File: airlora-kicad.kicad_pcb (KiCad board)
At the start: 4 copper layers, 77 x 77 mm, 168 parts, among them IC1 BALFHB-WL-02D3, J1 12V, J10 I2C, J11 UART2, J2 Conn_Coaxial, J3 Led, J4 SHT, J5 I2C, J6 A_NO2, J7 UART1, J8 A_CO, J9 I2C, Q10 S8050, Q2 S8050, Q3 S8050, Q4 S8050, Q5 S8050, Q6 S8050, Q7 S8050, Q8 S8050, Q9 S8050, SW1 SW_Push, SW2 SW_Slide_DPDT, SW3 SW_Push, U1 TPS7A2633DRVR, U2 TPS54202DDC, U3 TPS7A2633DRVR, U4 BGS12WN6E6327, U6 STM32F103C8Tx, U7 STM32WLE5CCUx, X1 32MHZ, Y1 32.768kHz, Y2 8Mhz

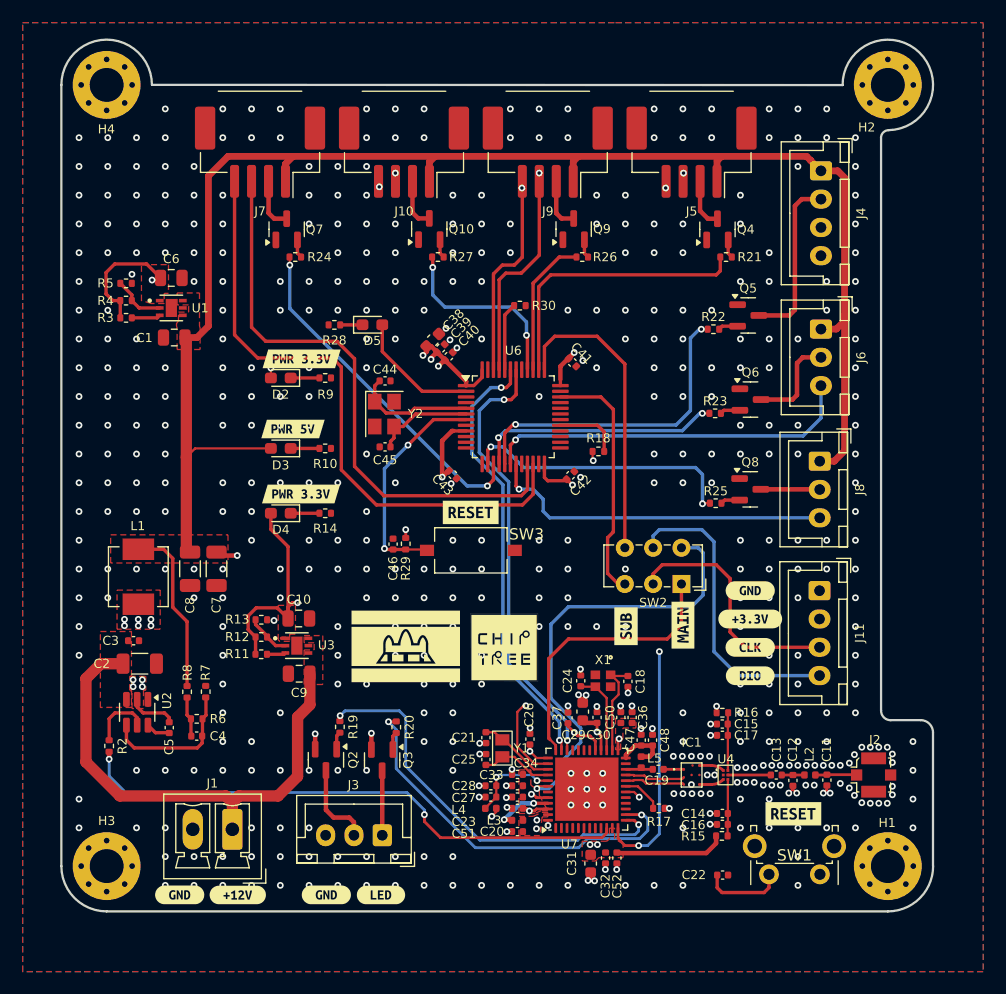
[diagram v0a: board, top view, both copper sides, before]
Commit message: Update trace and vias for power
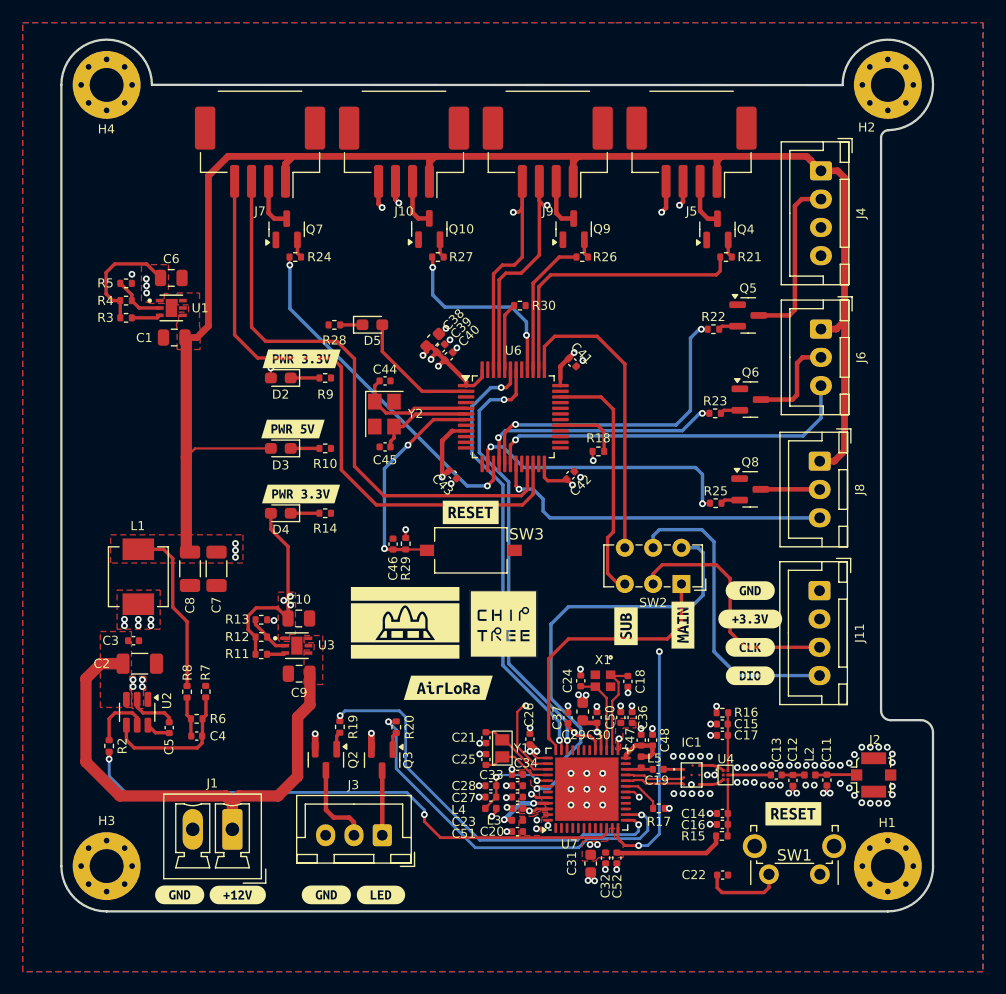
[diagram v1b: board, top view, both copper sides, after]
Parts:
- added kibuzzard-6679349C: G***, kibuzzard-6679349C, F.Cu at (94.7, 105.0)
- moved G*** 2.08 mm to (90.9, 99.3)
- moved G*** 2.08 mm to (99.6, 99.4)
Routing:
- net +3.3V_HP: track 74.7 -> 83.4 mm, vias 9 -> 11
- net /AirLora V3/MCU Sub/SDA1: track 61.7 -> 67.5 mm
- net +3.3V: track 106.0 -> 109.5 mm, vias 8 -> 11
- net /AirLora V3/MCU Sub/SCL1: track 60.7 -> 63.9 mm
- net +5V: track 186.8 -> 189.4 mm, vias 3 -> 5
- net GND: vias 484 -> 102

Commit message: Update power size track and add more vias
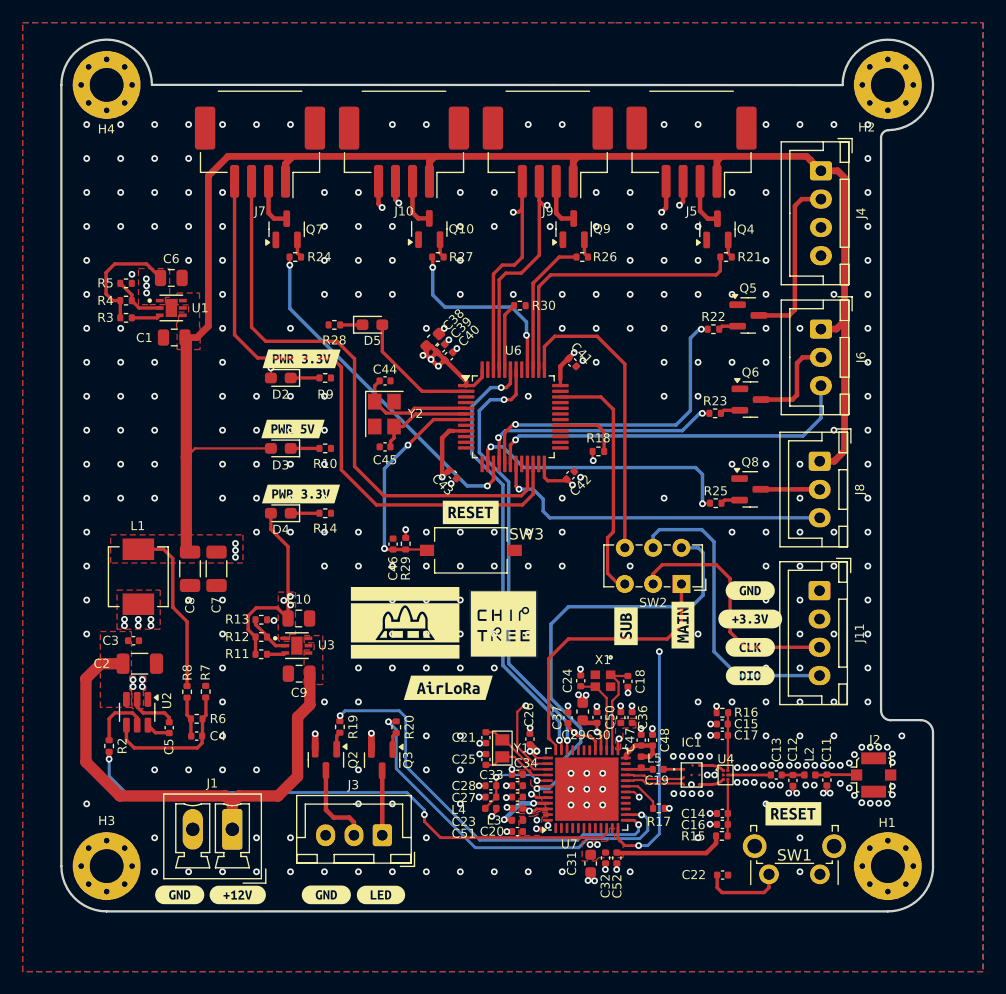
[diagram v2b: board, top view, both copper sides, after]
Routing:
- net +3.3V_HP: track 83.4 -> 85.3 mm
- net GND: vias 102 -> 357

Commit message: [Fix] Adjust layout power trace
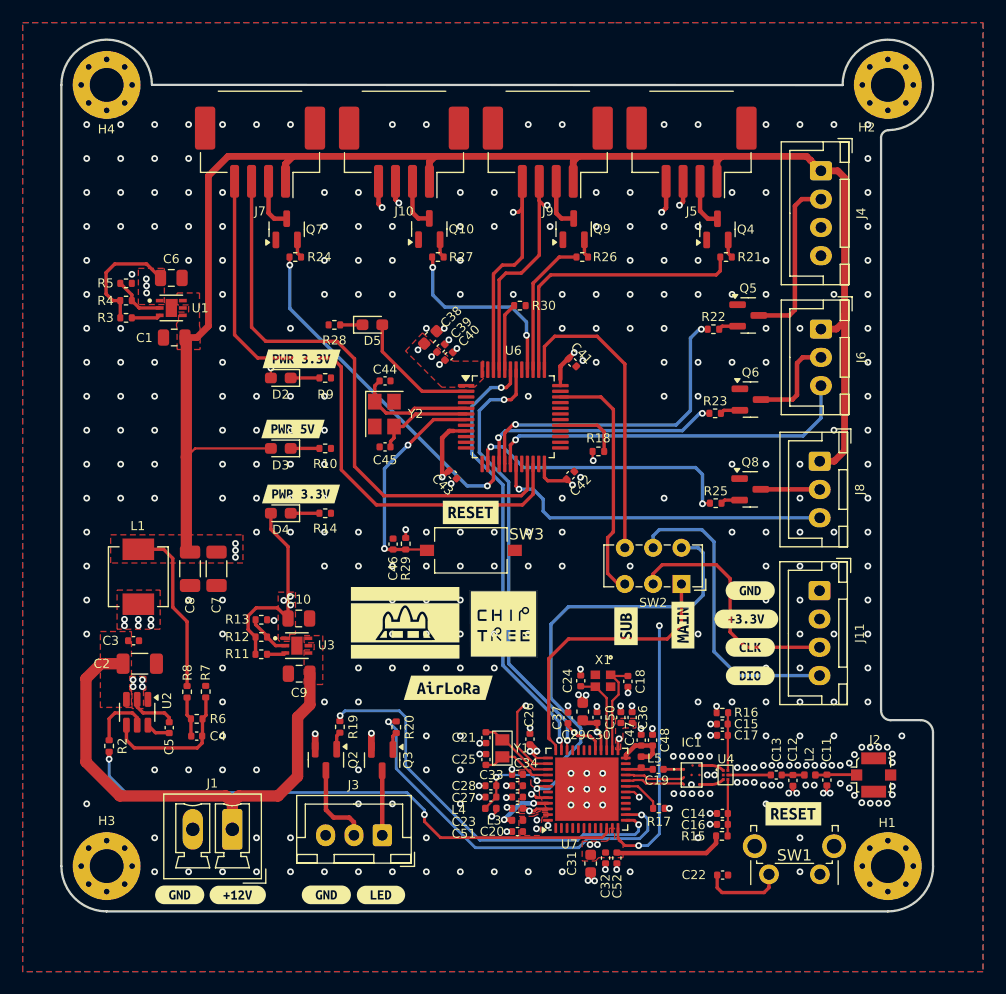
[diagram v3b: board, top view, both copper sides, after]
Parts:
- moved kibuzzard-66752939 0.35 mm to (121.0, 99.0)
- moved C38 0.32 mm to (93.1, 74.1)
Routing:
- net +3.3V: track 109.5 -> 40.4 mm
- net +3.3V_HP: track 85.3 -> 36.0 mm
- net +5V: track 189.4 -> 157.8 mm
- net /AirLora V3/MCU/NRST: track 26.1 -> 25.4 mm
- added copper zone on In2.Cu, net +5V

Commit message: Update inductor
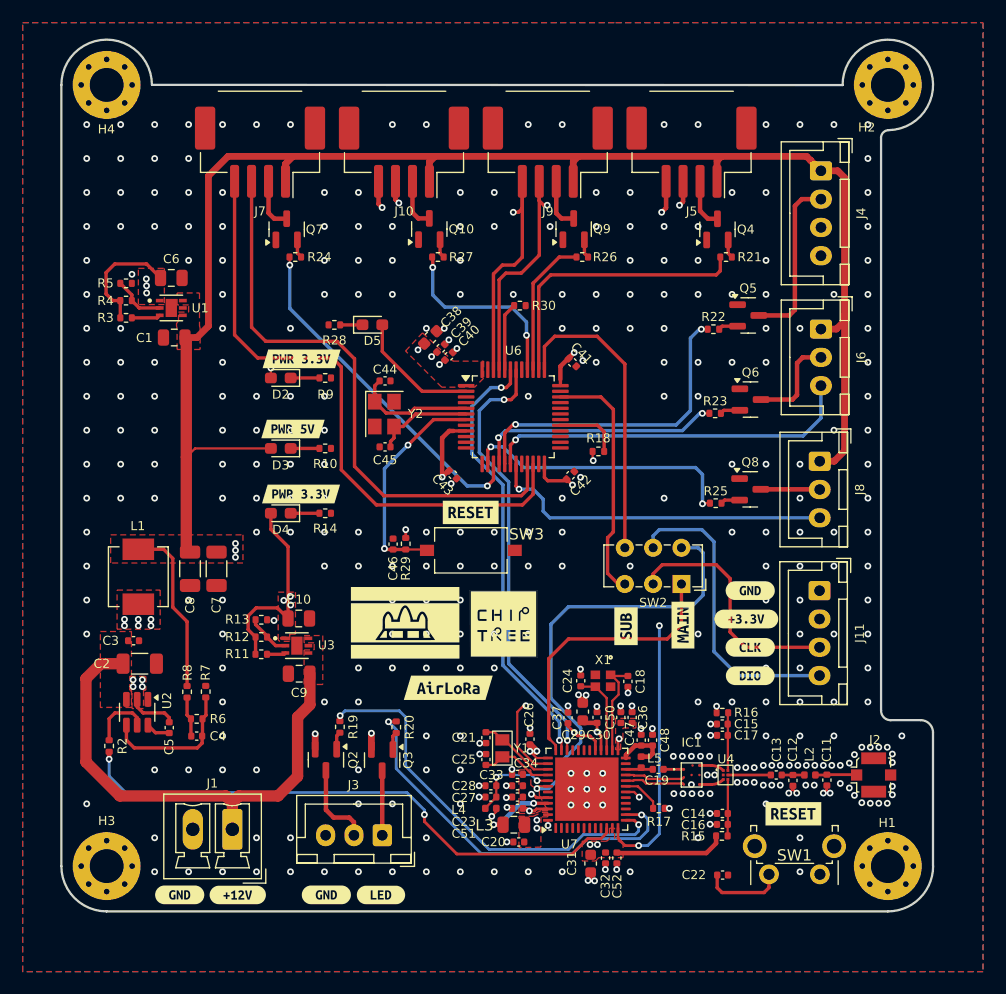
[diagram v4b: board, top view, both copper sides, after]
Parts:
- L3: footprint Inductor_SMD:L_0402_1005Metric -> Capacitor_SMD:C_0805_2012Metric
- moved C20 0.92 mm to (100.9, 118.7)
- moved L3 0.50 mm to (100.5, 117.1)
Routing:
- net Net-(U7-VFBSMPS): track 5.16 -> 6.40 mm
- net /AirLora V3/MCU/PA3: track 49.5 -> 50.7 mm
- net /AirLora V3/MCU/PA5: track 36.5 -> 37.2 mm

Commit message: update problem
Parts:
- removed Q10: S8050, Package_TO_SOT_SMD:SOT-23
- removed the Q4 at (118.5, 64.6)
- removed the kibuzzard-66752922 at (104.2, 55.6)
- removed the kibuzzard-66752922 at (91.6, 55.6)
- removed the kibuzzard-667540EB at (105.9, 55.6)
- removed the kibuzzard-667540EB at (93.3, 55.6)
- removed the kibuzzard-667541E6 at (100.9, 55.3)
- removed the kibuzzard-667541E6 at (88.3, 55.3)
- removed the kibuzzard-667541EF at (102.5, 55.3)
- removed the kibuzzard-667541EF at (89.9, 55.3)
- added J12: UART_MAIN, Connector_JST:JST_XH_B4B-XH-A_1x04_P2.50mm_Vertical, F.Cu at (66.5, 79.2)
- added Q2: S8050, Package_TO_SOT_SMD:SOT-23, F.Cu at (88.9, 111.5)
- added Q5: S8050, Package_TO_SOT_SMD:SOT-23, F.Cu at (121.3, 79.6)
- added kibuzzard-66752922: G***, kibuzzard-66752922, B.Cu at (87.7, 55.4)
- added kibuzzard-66752922: G***, kibuzzard-66752922, B.Cu at (101.4, 55.4)
- added kibuzzard-667540EB: G***, kibuzzard-667540EB, B.Cu at (85.7, 55.4)
- added kibuzzard-667540EB: G***, kibuzzard-667540EB, B.Cu at (99.5, 55.4)
- added kibuzzard-667541E6: G***, kibuzzard-667541E6, B.Cu at (91.6, 55.4)
- added kibuzzard-667541E6: G***, kibuzzard-667541E6, B.Cu at (105.4, 55.4)
- added kibuzzard-667541EF: G***, kibuzzard-667541EF, B.Cu at (89.6, 55.4)
- added kibuzzard-667541EF: G***, kibuzzard-667541EF, B.Cu at (103.4, 55.4)
- added kibuzzard-668CA440: G***, kibuzzard-668CA440, F.Cu at (77.9, 64.0)
- added kibuzzard-668CA458: G***, kibuzzard-668CA458, F.Cu at (91.6, 64.0)
- added kibuzzard-668CA46A: G***, kibuzzard-668CA46A, F.Cu at (105.2, 64.0)
- added kibuzzard-668CA479: G***, kibuzzard-668CA479, F.Cu at (119.2, 64.0)
- added kibuzzard-668CA498: G***, kibuzzard-668CA498, F.Cu at (117.2, 72.7)
- added kibuzzard-668CA4A7: G***, kibuzzard-668CA4A7, F.Cu at (117.2, 80.0)
- added kibuzzard-668CA4B6: G***, kibuzzard-668CA4B6, F.Cu at (117.3, 88.1)
- added kibuzzard-668CA4DF: G***, kibuzzard-668CA4DF, F.Cu at (83.9, 106.7)
- added kibuzzard-668CA658: G***, kibuzzard-668CA658, F.Cu at (88.8, 106.7)
- added kibuzzard-668CA679: G***, kibuzzard-668CA679, F.Cu at (87.0, 71.1)
- added kibuzzard-668F38B2: G***, kibuzzard-668F38B2, F.Cu at (67.7, 111.6)
- added kibuzzard-6690D059: G***, kibuzzard-6690D059, F.Cu at (73.0, 79.3)
- added kibuzzard-6690D084: G***, kibuzzard-6690D084, F.Cu at (73.0, 82.0)
- added kibuzzard-6690D08F: G***, kibuzzard-6690D08F, F.Cu at (73.0, 84.6)
- added kibuzzard-6690D099: G***, kibuzzard-6690D099, F.Cu at (73.0, 87.1)
- J10, J5, J7, J9: footprint Connector_Molex:Molex_CLIK-Mate_502585-0470_1x04-1MP_P1.50mm_Horizontal -> Connector_Molex:Molex_CLIK-Mate_502443-0470_1x04-1MP_P2.00mm_Vertical
- moved Q3 53.7 mm to (115.1, 64.6), turned to 90 degrees
- moved Q6 49.9 mm to (73.8, 64.6), turned to 90 degrees
- moved Q7 46.7 mm to (121.1, 87.5), turned to 0 degrees
- moved Q8 30.4 mm to (101.4, 64.6), turned to 90 degrees
- moved Q9 18.1 mm to (87.6, 64.6)
- moved kibuzzard-667540EB 8.84 mm to (71.6, 55.6)
- moved R23 8.13 mm to (73.1, 67.1), turned to 180 degrees
- moved R26 6.91 mm to (86.9, 67.1), turned to 180 degrees
- moved R25 5.89 mm to (100.7, 67.1), turned to 180 degrees
- moved kibuzzard-667541E6 5.64 mm to (119.1, 55.5)
- moved kibuzzard-667540EB 5.28 mm to (113.2, 55.5)
- moved kibuzzard-66752922 5.09 mm to (73.7, 55.6)
- moved R20 4.93 mm to (114.3, 67.1), turned to 180 degrees
- moved J7 3.24 mm to (74.8, 57.6), turned to 0 degrees
- moved kibuzzard-66752971 2.53 mm to (121.0, 101.5)
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- renumbered C15 to C14, C17 to C15, C14 to C16, C31 to C17, C16 to C18, C23 to C19, C32 to C20, C51 to C21, C52 to C22, C33 to C23, C27 to C24, C34 to C25, C28 to C26, C20 to C27, C22 to C28, C19 to C29, C47 to C30, C48 to C31, C26 to C32, C21 to C33, C37 to C34, C30 to C35, C25 to C36, C18 to C37, C36 to C38, C29 to C39, C50 to C40, C24 to C41, C38 to C42, C39 to C43, C40 to C44, C41 to C45, C42 to C46, C43 to C47, C44 to C48, C45 to C49, C46 to C50, D2 to D1, D3 to D2, D4 to D3, D5 to D4, L4 to L3, L3 to L4, Q2 to Q1, Q5 to Q4, R2 to R1, R11 to R10, R12 to R11, R13 to R12, R14 to R13, R16 to R14, R18 to R16, R19 to R18, R20 to R19, R3 to R2, R21 to R20, R22 to R21, R23 to R22, R24 to R23, R25 to R24, R26 to R25, R27 to R26, R28 to R27, R29 to R28, R30 to R29, R4 to R3, R5 to R4, R6 to R5, R7 to R6, R8 to R7, R9 to R8, R10 to R9, U7 to U5
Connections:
- Q1 pad 2: +5V -> Net-(J3-Pin_2)
- Q1 pad 3: Net-(J3-Pin_2) -> +5V
- Q3 pad 2: +5V -> GND
- Q3 pad 3: Net-(J3-Pin_1) -> Net-(J5-Pin_2)
- Q4 pad 1: GND -> Net-(Q4-B)
- Q4 pad 2: Net-(Q5-B) -> GND
- Q6 pad 1: GND -> Net-(Q6-B)
- Q6 pad 2: Net-(Q6-B) -> GND
- Q6 pad 3: Net-(J6-Pin_2) -> Net-(J7-Pin_2)
- Q7 pad 1: GND -> Net-(Q7-B)
- Q7 pad 2: Net-(Q7-B) -> GND
- Q7 pad 3: Net-(J7-Pin_2) -> Net-(J8-Pin_2)
- Q8 pad 1: GND -> Net-(Q8-B)
- Q8 pad 2: Net-(Q8-B) -> GND
- Q8 pad 3: Net-(J8-Pin_2) -> Net-(J9-Pin_2)
- Q9 pad 1: GND -> Net-(Q9-B)
- Q9 pad 2: Net-(Q9-B) -> GND
- Q9 pad 3: Net-(J9-Pin_2) -> Net-(J10-Pin_2)
- R19 pad 2: Net-(Q3-B) -> Net-(Q2-B)
- R20 pad 2: Net-(Q4-B) -> Net-(Q3-B)
- R21 pad 1: Net-(Q5-B) -> Net-(Q4-B)
- R22 pad 2: Net-(Q6-B) -> Net-(Q5-B)
- R23 pad 2: Net-(Q7-B) -> Net-(Q6-B)
- R24 pad 2: Net-(Q8-B) -> Net-(Q7-B)
- R25 pad 2: Net-(Q9-B) -> Net-(Q8-B)
- R26 pad 2: Net-(Q10-B) -> Net-(Q9-B)
- U5 pad 4: unconnected-(U7-PB6-Pad4) -> /AirLora V3/MCU/UART1_TX
- U5 pad 5: unconnected-(U7-PB7-Pad5) -> /AirLora V3/MCU/UART1_RX
- U6 pad 21: /AirLora V3/MCU Sub/TX3 -> /AirLora V3/MCU Sub/SCL2
- U6 pad 22: /AirLora V3/MCU Sub/RX3 -> /AirLora V3/MCU Sub/SDA2
- U6 pad 30: unconnected-(U6-PA9-Pad30) -> /AirLora V3/MCU Sub/TX3
- U6 pad 31: unconnected-(U6-PA10-Pad31) -> /AirLora V3/MCU Sub/RX3
- U6 pad 42: /AirLora V3/MCU Sub/SCL2 -> /AirLora V3/MCU Sub/SCL1
- U6 pad 43: /AirLora V3/MCU Sub/SDA2 -> /AirLora V3/MCU Sub/SDA1
- U6 pad 45: /AirLora V3/MCU Sub/SCL1 -> unconnected-(U6-PB8-Pad45)
- U6 pad 46: /AirLora V3/MCU Sub/SDA1 -> unconnected-(U6-PB9-Pad46)
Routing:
- net /AirLora V3/MCU/NRST: track 25.4 -> 114.6 mm
- net /AirLora V3/MCU/UART1_RX: track 0.00 -> 72.9 mm, vias 0 -> 1
- net /AirLora V3/MCU/UART1_TX: track 0.00 -> 71.7 mm, vias 0 -> 1
- net /AirLora V3/MCU Sub/SCL2: track 39.3 -> 26.9 mm
- net /AirLora V3/MCU Sub/SDA2: track 39.1 -> 26.8 mm
- net +5V: track 157.8 -> 169.5 mm
- net /AirLora V3/MCU Sub/PA5: track 30.7 -> 41.6 mm
- net /AirLora V3/MCU/PA5: track 37.2 -> 46.1 mm
- net /AirLora V3/MCU/PA6: track 34.4 -> 42.7 mm
- net /AirLora V3/MCU Sub/PB4: track 16.9 -> 23.8 mm
- net /AirLora V3/MCU Sub/RX3: track 54.6 -> 48.9 mm, vias 0 -> 2
- net /AirLora V3/MCU Sub/SDA1: track 67.5 -> 62.6 mm, vias 3 -> 4
- net /AirLora V3/MCU Sub/PA15: track 25.2 -> 21.5 mm
- net /AirLora V3/MCU Sub/SCL1: track 63.9 -> 60.4 mm, vias 3 -> 4
- net Net-(J3-Pin_2): track 7.95 -> 11.0 mm
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
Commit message: Update schematic
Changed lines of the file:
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@@
 	)
 	(segment
+		(start 73.370858 71.973658)
+		(end 71.450658 73.893858)
+		(width 0.6)
+		(layer "F.Cu")
+		(net 4)
+	)
+	(segment
+		(start 80.076458 71.973658)
+		(end 73.370858 71.973658)
+		(width 0.6)
+		(layer "F.Cu")
+		(net 4)
+	)
+	(segment
 		(start 127.625258 59.380458)
 		(end 126.492058 58.247258)
@@
 	)
 	(segment
-		(start 81.651258 70.398858)
-		(end 79.212858 72.837258)
-		(width 0.6)
-		(layer "F.Cu")
-		(net 4)
-	)
-	(segment
 		(start 129.708058 84.114858)
 		(end 128.794458 85.028458)
@@
 	)
 	(segment
-		(start 79.212858 72.837258)
-		(end 74.488458 72.837258)
-		(width 0.6)
-		(layer "F.Cu")
-		(net 4)
-	)
-	(segment
 		(start 84.666258 112.341858)
 		(end 84.699258 112.308858)
@@
 	)
 	(segment
+		(start 71.450658 73.893858)
+		(end 71.450658 74.105)
+		(width 0.6)
+		(layer "F.Cu")
+		(net 4)
+	)
+	(segment
 		(start 113.858458 58.247258)
 		(end 100.294858 58.247258)
@@
 	)
 	(segment
-		(start 74.488458 72.837258)
-		(end 73.220716 74.105)
-		(width 0.6)
-		(layer "F.Cu")
-		(net 4)
-	)
-	(segment
 		(start 83.900558 112.341858)
 		(end 84.666258 112.341858)
@@
 	)
 	(segment
-		(start 80.686058 58.247258)
-		(end 81.651258 59.212458)
+		(start 81.651258 70.398858)
+		(end 80.076458 71.973658)
 		(width 0.6)
 		(layer "F.Cu")
@@
 	)
 	(segment
-		(start 73.220716 74.105)
-		(end 71.450658 74.105)
+		(start 80.686058 58.247258)
+		(end 81.651258 59.212458)
 		(width 0.6)
 		(layer "F.Cu")
@@
 	)
 	(zone
-		(net 6)
-		(net_name "Net-(J2-In)")
-		(layer "F.Cu")
-		(name "$teardrop_padvia$")
-		(hatch full 0.1)
-		(priority 30000)
-		(attr
-			(teardrop
-				(type padvia)
-			)
-		)
-		(connect_pads yes
-			(clearance 0)
-		)
-		(min_thickness 0.0254)
-		(filled_areas_thickness no)
-		(fill yes
-			(thermal_gap 0.5)
-			(thermal_bridge_width 0.5)
-			(island_removal_mode 1)
-			(island_area_min 10)
-		)
-		(polygon
-			(pts
-				(xy 129.7776 112.839) (xy 129.8776 112.878987) (xy 129.9776 112.938002) (xy 130.077599 113.016043)
-				(xy 130.177599 113.113112) (xy 130.2776 113.229209) (xy 130.7786 112.744) (xy 130.2776 112.244)
-				(xy 130.177599 112.349448) (xy 130.077599 112.436672) (xy 129.9776 112.505672) (xy 129.8776 112.556448)
-				(xy 129.7776 112.589)
-			)
-		)
-	)
-	(zone
 		(net 25)
 		(net_name "+3.3V_HP")
@@
 			)
 		)
+	)
+	(zone
+		(net 6)
+		(net_name "Net-(J2-In)")
+		(layer "F.Cu")
+		(name "$teardrop_padvia$")
+		(hatch full 0.1)
+		(priority 30000)
+		(attr
+			(teardrop
+				(type padvia)
+			)
+		)
+		(connect_pads yes
+			(clearance 0)
+		)
+		(min_thickness 0.0254)
+		(filled_areas_thickness no)
+		(fill yes
+			(thermal_gap 0.5)
+			(thermal_bridge_width 0.5)
+			(island_removal_mode 1)
+			(island_area_min 10)
+		)
+		(polygon
+			(pts
+				(xy 129.7776 112.839) (xy 129.8776 112.878987) (xy 129.9776 112.938002) (xy 130.077599 113.016043)
+				(xy 130.177599 113.113112) (xy 130.2776 113.229209) (xy 130.7786 112.744) (xy 130.2776 112.244)
+				(xy 130.177599 112.349448) (xy 130.077599 112.436672) (xy 129.9776 112.505672) (xy 129.8776 112.556448)
+				(xy 129.7776 112.589)
+			)
+		)
